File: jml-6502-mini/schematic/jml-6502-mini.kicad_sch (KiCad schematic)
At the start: 4 parts

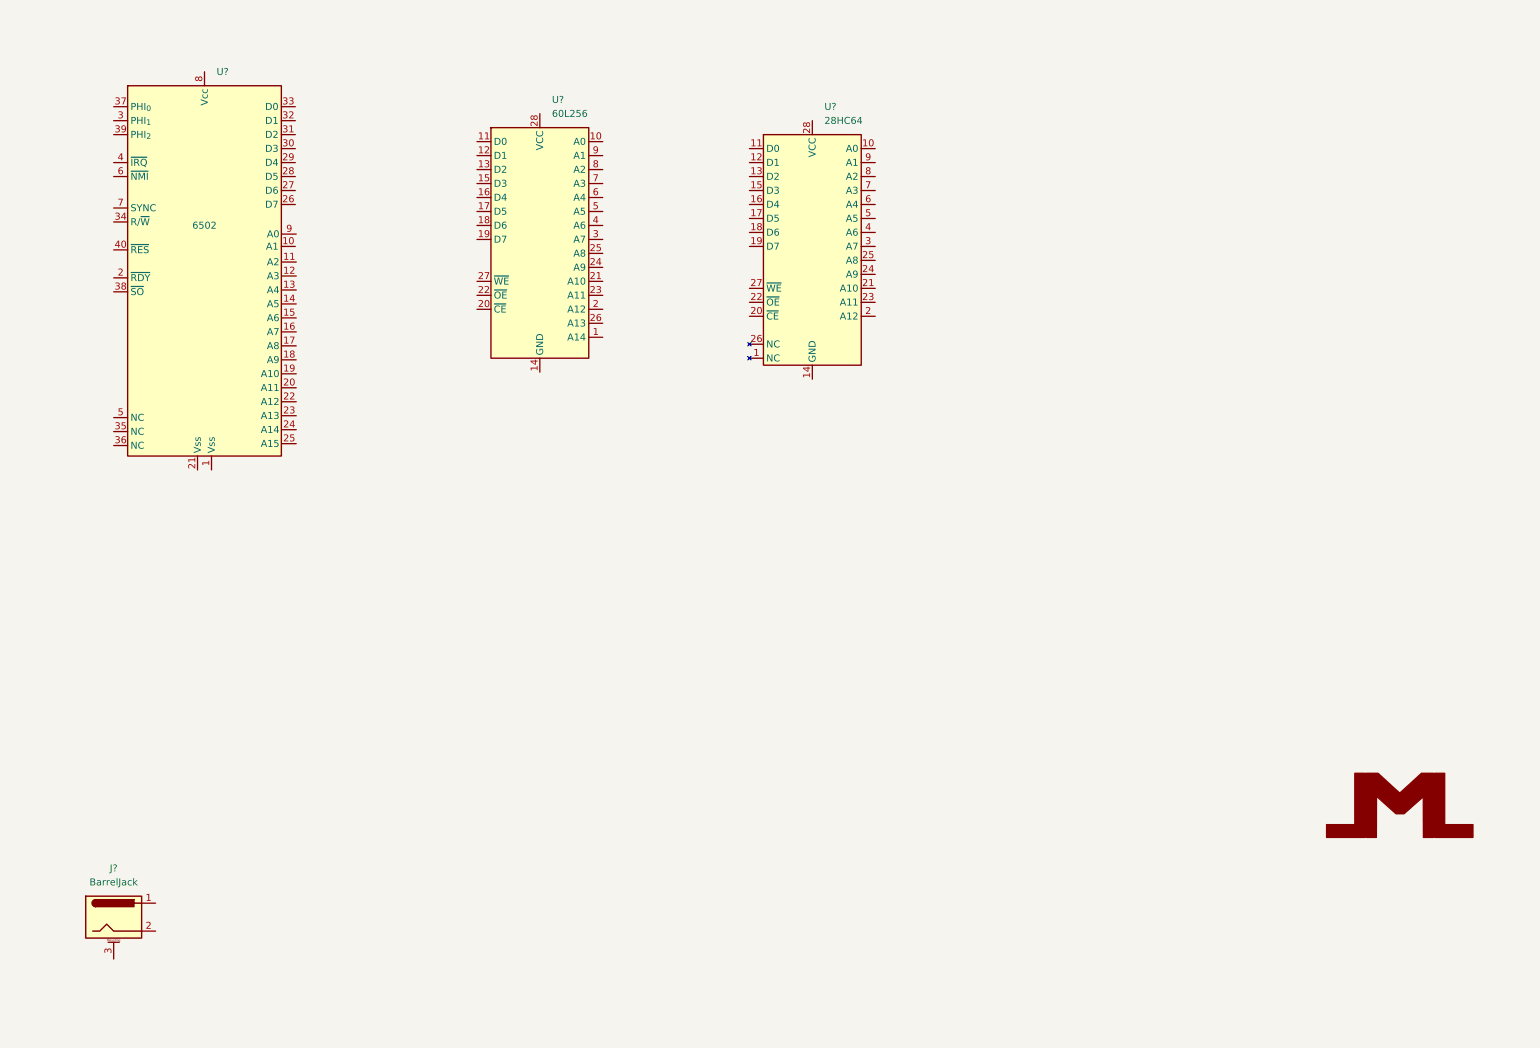
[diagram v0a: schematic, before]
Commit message: complete jml-6502-mini schematic
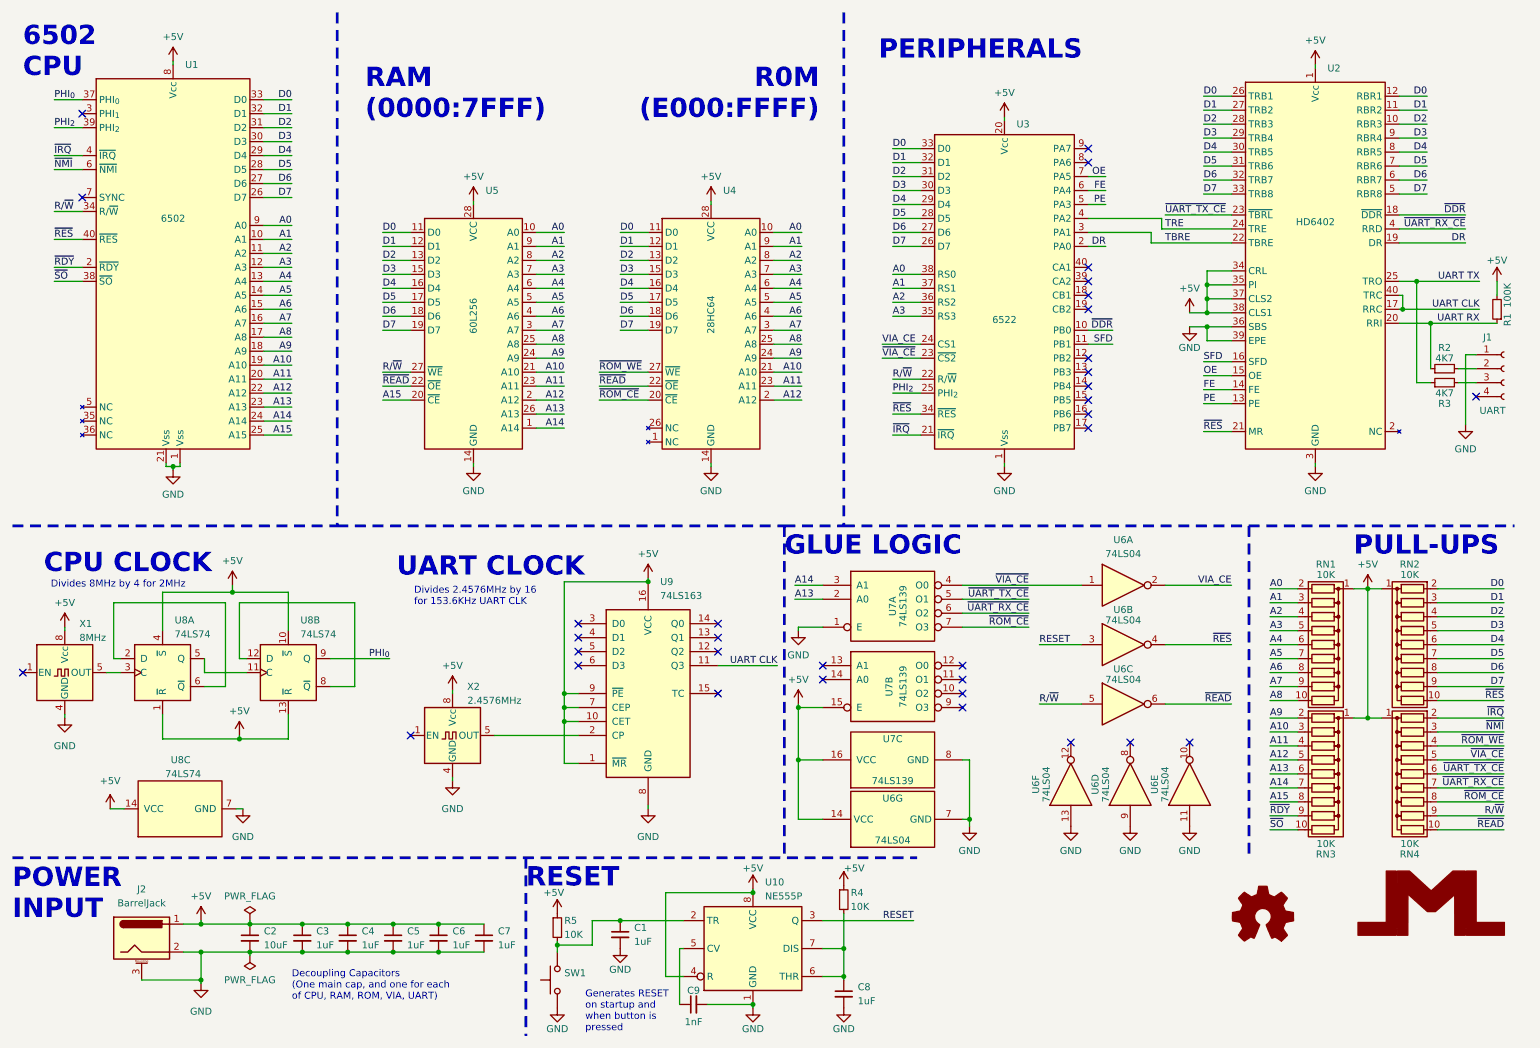
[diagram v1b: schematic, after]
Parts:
- added C1, C3, C4, C5, C6, C7, C8: 1uF, symbol Device:C_Small
- added C2: 10uF, symbol Device:C_Small
- added C9: 1nF, symbol Device:C_Small
- added J1: UART, symbol Connector:Conn_01x04_Socket
- added R1: 100K, symbol Device:R_Small
- added R2, R3: 4K7, symbol Device:R_Small
- added R4, R5: 10K, symbol Device:R_Small
- added RN1, RN2, RN3, RN4: 10K, Resistor_THT:R_Array_SIP10, symbol Device:R_Network09
- added SW1: ~, symbol Switch:SW_Push
- added U10: NE555P, Package_DIP:DIP-8_W7.62mm, symbol Timer:NE555P
- added U2: HD6402, symbol JML:HD6402
- added U3: 6522, symbol JML:6522
- added U6: 74LS04, symbol 74xx:74LS04
- added U7: 74LS139, symbol 74xx:74LS139
- added U8: 74LS74, symbol 74xx:74LS74
- added U9: 74LS163, symbol 74xx:74LS163
- added X1: 8MHz, Oscillator:Oscillator_DIP-8, symbol Oscillator:CXO_DIP8
- added X2: 2.4576MHz, Oscillator:Oscillator_DIP-8, symbol Oscillator:CXO_DIP8
- gave numbers to parts that had none: 4
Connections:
- net A0: now reaches U4.10 (A0)
- net A0: now also U1.9 (A0), U5.10 (A0), RN1.2 (R1), U3.38 (RS0)
- net D0: now reaches U4.11 (D0)
- net D0: now also U1.33 (D0), U5.11 (D0), RN2.2 (R1), U2.12 (RBR1), U2.26 (TRB1), U3.33 (D0)
- net D1: now reaches U4.12 (D1)
- net D1: now also U1.32 (D1), U5.12 (D1), RN2.3 (R2), U2.11 (RBR2), U2.27 (TRB2), U3.32 (D1)
- net D2: now reaches U4.13 (D2)
- net D2: now also U1.31 (D2), U5.13 (D2), RN2.4 (R3), U2.10 (RBR3), U2.28 (TRB3), U3.31 (D2)
- net GND: now reaches U4.14 (GND)
- net GND: now also J2.2, J2.3 (MountPin), U1.1 (Vss), U1.21 (Vss), U5.14 (GND), C1.2, C2.2, C3.2, C4.2, C5.2, C6.2, C7.2, C8.2, C9.2, J1.1 (Pin_1), SW1.1, U10.1 (GND), U2.3 (GND), U2.36 (SBS), U2.39 (EPE), U3.1 (Vss), U6.11, U6.13, U6.7 (GND), U6.9, U7.1 (E), U7.8 (GND), U8.7 (GND), U9.8 (GND), X1.4 (GND), X2.4 (GND)
- net D3: now reaches U4.15 (D3)
- net D3: now also U1.30 (D3), U5.15 (D3), RN2.5 (R4), U2.29 (TRB4), U2.9 (RBR4), U3.30 (D3)
- net D4: now reaches U4.16 (D4)
- net D4: now also U1.29 (D4), U5.16 (D4), RN2.6 (R5), U2.30 (TRB5), U2.8 (RBR5), U3.29 (D4)
- net D5: now reaches U4.17 (D5)
- net D5: now also U1.28 (D5), U5.17 (D5), RN2.7 (R6), U2.31 (TRB6), U2.7 (RBR6), U3.28 (D5)
- net D6: now reaches U4.18 (D6)
- net D6: now also U1.27 (D6), U5.18 (D6), RN2.8 (R7), U2.32 (TRB7), U2.6 (RBR7), U3.27 (D6)
- net D7: now reaches U4.19 (D7)
- net D7: now also U1.26 (D7), U5.19 (D7), RN2.9 (R8), U2.33 (TRB8), U2.5 (RBR8), U3.26 (D7)
- net A12: now reaches U4.2 (A12)
- net A12: now also U1.22 (A12), U5.2 (A12), RN3.5 (R4)
- net ~{ROM_CE}: now reaches U4.20 (~{CE})
- net ~{ROM_CE}: now also RN4.8 (R7), U7.7 (O3)
- net A10: now reaches U4.21 (A10)
- net A10: now also U1.19 (A10), U5.21 (A10), RN3.3 (R2)
- net ~{READ}: now reaches U4.22 (~{OE})
- net ~{READ}: now also U5.22 (~{OE}), RN4.10 (R9), U6.6
- net A11: now reaches U4.23 (A11)
- net A11: now also U1.20 (A11), U5.23 (A11), RN3.4 (R3)
- net A9: now reaches U4.24 (A9)
- net A9: now also U1.18 (A9), U5.24 (A9), RN3.2 (R1)
- net A8: now reaches U4.25 (A8)
- net A8: now also U1.17 (A8), U5.25 (A8), RN1.10 (R9)
- net ~{ROM_WE}: now reaches U4.27 (~{WE})
- net ~{ROM_WE}: now also RN4.4 (R3)
- net +5V: now reaches U4.28 (VCC)
- net +5V: now also J2.1, U1.8 (Vcc), U5.28 (VCC), C2.1, C3.1, C4.1, C5.1, C6.1, C7.1, R1.2, R4.1, R5.1, RN1.1 (common), RN2.1 (common), RN3.1 (common), RN4.1 (common), U10.4 (R), U10.8 (VCC), U2.1 (Vcc), U2.34 (CRL), U2.35 (PI), U2.37 (CLS2), U2.38 (CLS1), U3.20 (Vcc), U6.14 (VCC), U7.15 (E), U7.16 (VCC), U8.1 (~{R}), U8.10 (~{S}), U8.13 (~{R}), U8.14 (VCC), U8.4 (~{S}), U9.1 (~{MR}), U9.10 (CET), U9.16 (VCC), U9.7 (CEP), U9.9 (~{PE}), X1.8 (Vcc), X2.8 (Vcc)
- net A7: now reaches U4.3 (A7)
- net A7: now also U1.16 (A7), U5.3 (A7), RN1.9 (R8)
- net A6: now reaches U4.4 (A6)
- net A6: now also U1.15 (A6), U5.4 (A6), RN1.8 (R7)
- net A5: now reaches U4.5 (A5)
- net A5: now also U1.14 (A5), U5.5 (A5), RN1.7 (R6)
- net A4: now reaches U4.6 (A4)
- net A4: now also U1.13 (A4), U5.6 (A4), RN1.6 (R5)
- net A3: now reaches U4.7 (A3)
- net A3: now also U1.12 (A3), U5.7 (A3), RN1.5 (R4), U3.35 (RS3)
- net A2: now reaches U4.8 (A2)
- net A2: now also U1.11 (A2), U5.8 (A2), RN1.4 (R3), U3.36 (RS2)
- net A1: now reaches U4.9 (A1)
- net A1: now also U1.10 (A1), U5.9 (A1), RN1.3 (R2), U3.37 (RS1)
- net A14: now reaches U5.1 (A14)
- net A14: now also U1.24 (A14), RN3.7 (R6), U7.3 (A1)
- net A15: now reaches U5.20 (~{CE})
- net A15: now also U1.25 (A15), RN3.8 (R7)
- net A13: now reaches U5.26 (A13)
- net A13: now also U1.23 (A13), RN3.6 (R5), U7.2 (A0)
- net R/~{W}: now reaches U5.27 (~{WE})
- net R/~{W}: now also U1.34 (R/~{W}), RN4.9 (R8), U3.22 (R/~{W}), U6.5
- net ~{RDY}: now reaches U1.2 (~{RDY})
- net ~{RDY}: now also RN3.9 (R8)
- net PHI_{0}: now reaches U1.37 (PHI_{0})
- net PHI_{0}: now also U8.9 (Q)
- net ~{SO}: now reaches U1.38 (~{SO})
- net ~{SO}: now also RN3.10 (R9)
- net PHI_{2}: now reaches U1.39 (PHI_{2})
- net PHI_{2}: now also U3.25 (PHI_{2})
- net ~{IRQ}: now reaches U1.4 (~{IRQ})
- net ~{IRQ}: now also RN4.2 (R1), U3.21 (~{IRQ})
- net ~{RES}: now reaches U1.40 (~{RES})
- net ~{RES}: now also RN2.10 (R9), U2.21 (MR), U3.34 (~{RES}), U6.4
- net ~{NMI}: now reaches U1.6 (~{NMI})
- net ~{NMI}: now also RN4.3 (R2)
- new net: C1.1, R5.2, SW1.2, U10.2 (TR)
- new net: C9.1, U10.5 (CV)
- new net: C8.1, R4.2, U10.6 (THR), U10.7 (DIS)
- new net: U8.3 (C), X1.5 (OUT)
- new net: U9.2 (CP), X2.5 (OUT)
- new net: U8.2 (D), U8.6 (~{Q})
- new net: U8.11 (C), U8.5 (Q)
- new net: J1.2 (Pin_2), R2.2
- new net: U8.12 (D), U8.8 (~{Q})
- new net: J1.3 (Pin_3), R3.2
- new net DR: U2.19 (DR), U3.2 (PA0)
- new net FE: U2.14 (FE), U3.6 (PA4)
- new net OE: U2.15 (OE), U3.7 (PA5)
- new net PE: U2.13 (PE), U3.5 (PA3)
- new net RESET: U10.3 (Q), U6.3
- new net SFD: U2.16 (SFD), U3.11 (PB1)
- new net TBRE: U2.22 (TBRE), U3.3 (PA1)
- new net TRE: U2.24 (TRE), U3.4 (PA2)
- new net UART CLK: U2.17 (RRC), U2.40 (TRC), U9.11 (Q3)
- new net UART RX: R1.1, R2.1, U2.20 (RRI)
- new net UART TX: R3.1, U2.25 (TRO)
- new net VIA_CE: U3.24 (CS1), U6.2
- new net ~{DDR}: U2.18 (~{DDR}), U3.10 (PB0)
- new net ~{UART_RX_CE}: RN4.7 (R6), U2.4 (RRD), U7.6 (O2)
- new net ~{UART_TX_CE}: RN4.6 (R5), U2.23 (~{TBRL}), U7.5 (O1)
- new net ~{VIA_CE}: RN4.5 (R4), U3.23 (~{CS2}), U6.1, U7.4 (O0)
- no-connect marks 0 -> 34
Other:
- note added: "6502 CPU"
- note added: "CPU CLOCK"
- note added: "Decoupling Capacitors (One main cap, and one for each of CPU, RAM, ROM, VIA, UART)"
- note added: "Divides 2.4576MHz by 16 for 153.6KHz UART CLK"
- note added: "Divides 8MHz by 4 for 2MHz"
- note added: "GLUE LOGIC"
- note added: "Generates RESET on startup and when button is pressed"
- note added: "PERIPHERALS"
- note added: "POWER INPUT"
- note added: "PULL-UPS"
- note added: "R0M (E000:FFFF)"
- note added: "RAM (0000:7FFF)"
- note added: "RESET"
- note added: "UART CLOCK"
- moved on the sheet: J2, U4, U5

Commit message: begin working on pcb for jml-6502-mini
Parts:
- added H1, H2, H3, H4: MountingHole, MountingHole:MountingHole_2.7mm_M2.5, symbol Mechanical:MountingHole
- C1, C3, C4, C5, C6, C7, C8, C9: footprint (none) -> Capacitor_THT:C_Disc_D5.0mm_W2.5mm_P5.00mm
- C2: footprint (none) -> Capacitor_THT:C_Radial_D5.0mm_H11.0mm_P2.00mm
- J1: footprint (none) -> Connector_PinHeader_2.54mm:PinHeader_1x04_P2.54mm_Horizontal
- R1, R2, R3, R4, R5: footprint (none) -> Resistor_THT:R_Axial_DIN0207_L6.3mm_D2.5mm_P7.62mm_Horizontal
- SW1: footprint (none) -> Button_Switch_THT:SW_Tactile_Straight_KSA0Axx1LFTR
- U1, U2, U3: footprint (none) -> Package_DIP:DIP-40_W15.24mm_Socket_LongPads
- U10: footprint Package_DIP:DIP-8_W7.62mm -> Package_DIP:DIP-8_W7.62mm_Socket_LongPads
- U4, U5: footprint (none) -> Package_DIP:DIP-28_W15.24mm_Socket_LongPads
- U6, U8: footprint (none) -> Package_DIP:DIP-14_W7.62mm_Socket_LongPads
- U7, U9: footprint (none) -> Package_DIP:DIP-16_W7.62mm_Socket_LongPads
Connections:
- net A0: now also RN1.8 (R7); no longer RN1.2 (R1)
- net A1: now also RN1.9 (R8); no longer RN1.3 (R2)
- net A11: now also RN3.2 (R1); no longer RN3.4 (R3)
- net A12: now also RN4.2 (R1); no longer RN3.5 (R4)
- net A13: now also RN4.3 (R2); no longer RN3.6 (R5)
- net A14: now also RN4.4 (R3); no longer RN3.7 (R6)
- net A15: now also RN4.5 (R4); no longer RN3.8 (R7)
- net A2: now also RN1.10 (R9); no longer RN1.4 (R3)
- net A3: now also RN3.10 (R9); no longer RN1.5 (R4)
- net A4: now also RN3.9 (R8); no longer RN1.6 (R5)
- net A5: now also RN3.8 (R7); no longer RN1.7 (R6)
- net A6: now also RN3.7 (R6); no longer RN1.8 (R7)
- net A7: now also RN3.6 (R5); no longer RN1.9 (R8)
- net A8: now also RN3.5 (R4); no longer RN1.10 (R9)
- net A9: now also RN3.4 (R3); no longer RN3.2 (R1)
- net D0: now also RN2.8 (R7); no longer RN2.2 (R1)
- net D1: now also RN2.9 (R8); no longer RN2.3 (R2)
- net D2: now also RN2.10 (R9); no longer RN2.4 (R3)
- net D3: now also RN4.10 (R9); no longer RN2.5 (R4)
- net D4: now also RN4.9 (R8); no longer RN2.6 (R5)
- net D5: now also RN4.8 (R7); no longer RN2.7 (R6)
- net D6: now also RN4.7 (R6); no longer RN2.8 (R7)
- net D7: now also RN4.6 (R5); no longer RN2.9 (R8)
- net R/~{W}: now also RN1.7 (R6); no longer RN4.9 (R8)
- net ~{IRQ}: now also RN1.5 (R4); no longer RN4.2 (R1)
- net ~{NMI}: now also RN1.6 (R5); no longer RN4.3 (R2)
- net ~{RDY}: now also RN1.3 (R2); no longer RN3.9 (R8)
- net ~{READ}: now also RN2.7 (R6); no longer RN4.10 (R9)
- net ~{RES}: now also RN1.2 (R1); no longer RN2.10 (R9)
- net ~{ROM_CE}: now also RN2.6 (R5); no longer RN4.8 (R7)
- net ~{ROM_WE}: now also RN2.2 (R1); no longer RN4.4 (R3)
- net ~{SO}: now also RN1.4 (R3); no longer RN3.10 (R9)
- net ~{UART_RX_CE}: now also RN2.5 (R4); no longer RN4.7 (R6)
- net ~{UART_TX_CE}: now also RN2.4 (R3); no longer RN4.6 (R5)
- net ~{VIA_CE}: now also RN2.3 (R2); no longer RN4.5 (R4)
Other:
- moved on the sheet: C2, C3, C4, C5, C6, C7, J2
